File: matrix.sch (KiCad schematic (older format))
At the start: 179 parts, among them SW1.1 Backtick, SW1.10 9, SW1.11 0, SW1.12 -, SW1.13 =, SW1.2 1, SW1.3 2, SW1.4 3, SW1.5 4, SW1.6 5, SW1.7 6, SW1.8 7, SW1.9 8, SW2A1 Tab, SW2A10 I, SW2A11 O, SW2A12 P, SW2A13 /, SW2A2 Q, SW2A3 W, SW2A4 E, SW2A5 R, SW2A6 T, SW2A8 Y, SW2A9 U, SW2B1 Tab, SW2B10 I, SW2B11 O, SW2B12 P, SW2B13 /, SW2B2 Q, SW2B3 W, SW2B4 E, SW2B5 R, SW2B6 T, SW2B7 Y, SW2B8 Y, SW2B9 U, SW3A1 Bksp, SW3A10 K, SW3A11 L, SW3A12 ;, SW3A13 Enter, SW3A2 A, SW3A3 S, SW3A4 D, SW3A5 F, SW3A6 G, SW3A8 H, SW3A9 J, SW3B1 Bksp, SW3B10 K, SW3B11 L, SW3B12 ;, SW3B13 Enter, SW3B2 A, SW3B3 S, SW3B4 D, SW3B5 F, SW3B6 G, SW3B7 H, SW3B8 H, SW3B9 J, SW4A1 LShift, SW4A10 ,, SW4A11 ., SW4A13 RShift, SW4A3 Z, SW4A4 X, SW4A5 C, SW4A6 V, SW4A8 N, SW4A9 M, SW4B1 LShift, SW4B10 ,, SW4B11 ., SW4B12 ., SW4B13 RShift, SW4B2 Z, SW4B3 Z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

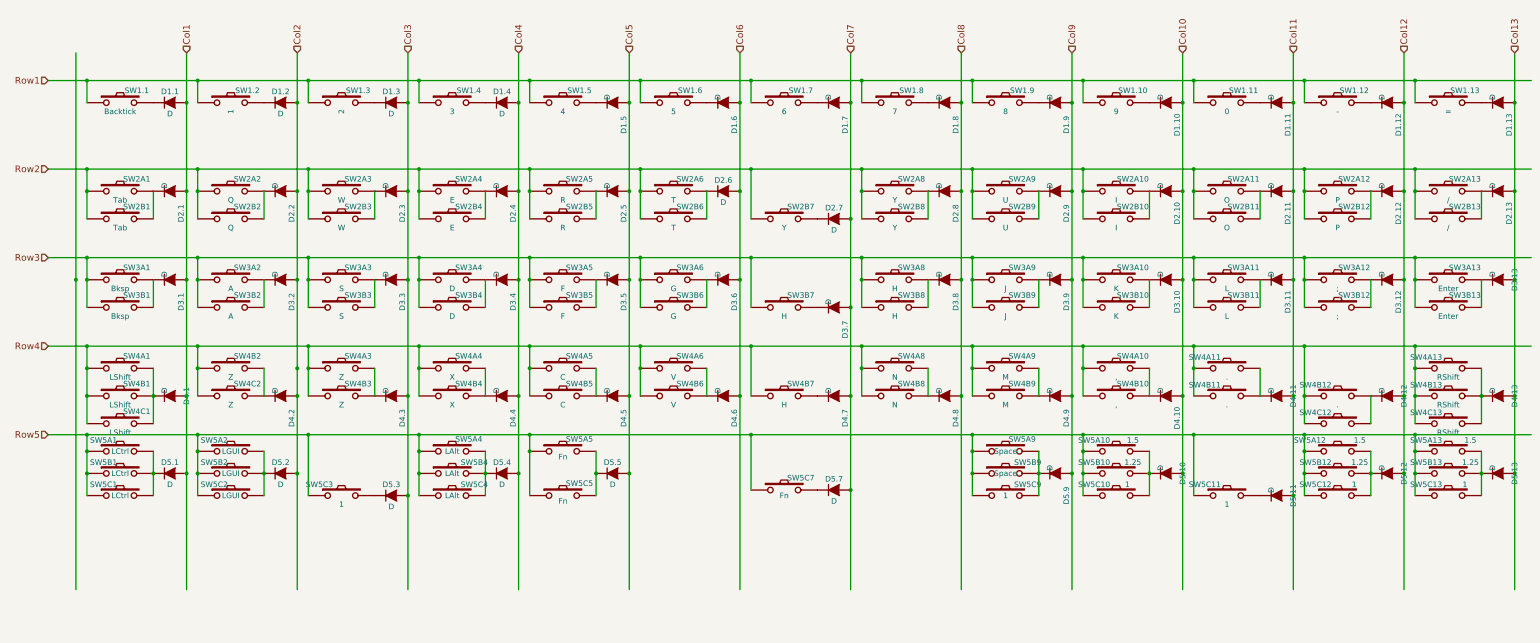
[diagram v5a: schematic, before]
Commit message: Focusing efforts on one main layout (semi-ortho), so that PCB-mounted and Alps components can be supported
Updated keenkeeb-reb1.png with new layout.
Started removing footprints and adding new spacebar footprints.
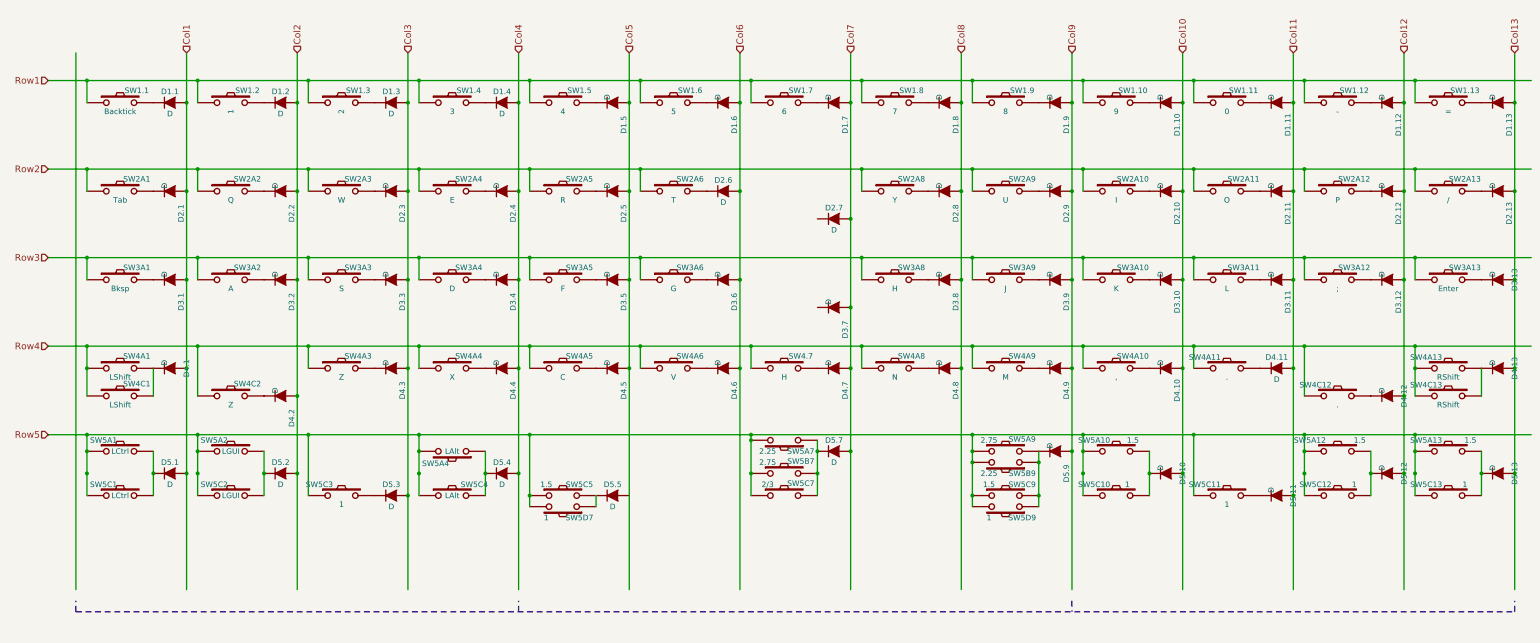
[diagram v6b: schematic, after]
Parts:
- removed SW2B1: Tab, footprints:MX_100_Plate, symbol SW_PUSH
- removed SW2B10: I, footprints:MX_100_Plate, symbol SW_PUSH
- removed SW2B11: O, footprints:MX_100_Plate, symbol SW_PUSH
- removed SW2B12: P, footprints:MX_100_Plate, symbol SW_PUSH
- removed SW2B13: /, footprints:MX_100_Plate, symbol SW_PUSH
- removed SW2B2: Q, footprints:MX_100_Plate, symbol SW_PUSH
- removed SW2B3: W, footprints:MX_100_Plate, symbol SW_PUSH
- removed SW2B4: E, footprints:MX_100_Plate, symbol SW_PUSH
- removed SW2B5: R, footprints:MX_100_Plate, symbol SW_PUSH
- removed SW2B6: T, footprints:MX_100_Plate, symbol SW_PUSH
- removed SW2B7, SW2B8: Y, footprints:MX_100_Plate, symbol SW_PUSH
- removed SW2B9: U, footprints:MX_100_Plate, symbol SW_PUSH
- removed SW3B1: Bksp, footprints:MX_100_Plate, symbol SW_PUSH
- removed SW3B10: K, footprints:MX_100_Plate, symbol SW_PUSH
- removed SW3B11: L, footprints:MX_100_Plate, symbol SW_PUSH
- removed SW3B12: ;, footprints:MX_100_Plate, symbol SW_PUSH
- removed SW3B13: Enter, footprints:MX_100_Plate, symbol SW_PUSH
- removed SW3B2: A, footprints:MX_100_Plate, symbol SW_PUSH
- removed SW3B3: S, footprints:MX_100_Plate, symbol SW_PUSH
- removed SW3B4: D, footprints:MX_100_Plate, symbol SW_PUSH
- removed SW3B5: F, footprints:MX_100_Plate, symbol SW_PUSH
- removed SW3B6: G, footprints:MX_100_Plate, symbol SW_PUSH
- removed SW3B7, SW3B8: H, footprints:MX_100_Plate, symbol SW_PUSH
- removed SW3B9: J, footprints:MX_100_Plate, symbol SW_PUSH
- removed SW4B1: LShift, footprints:MX_150_Plate, symbol SW_PUSH
- removed SW4B10: ,, footprints:MX_100_Plate, symbol SW_PUSH
- removed SW4B11, SW4B12: ., footprints:MX_100_Plate, symbol SW_PUSH
- removed SW4B13: RShift, footprints:MX_150_Plate, symbol SW_PUSH
- removed SW4B3, SW4C2: Z, footprints:MX_100_Plate, symbol SW_PUSH
- removed SW4B4: X, footprints:MX_100_Plate, symbol SW_PUSH
- removed SW4B5: C, footprints:MX_100_Plate, symbol SW_PUSH
- removed SW4B6: V, footprints:MX_100_Plate, symbol SW_PUSH
- removed SW4B8: N, footprints:MX_100_Plate, symbol SW_PUSH
- removed SW4B9: M, footprints:MX_100_Plate, symbol SW_PUSH
- removed SW5B1: LCtrl, footprints:MX_125_Plate, symbol SW_PUSH
- removed SW5B10, SW5B12, SW5B13: 1.25, footprints:MX_125_Plate, symbol SW_PUSH
- removed SW5B2: LGUI, footprints:MX_125_Plate, symbol SW_PUSH
- removed SW5B4: LAlt, footprints:MX_125_Plate, symbol SW_PUSH
- added SW5C5: 1.5, footprints:MX_150_Plate, symbol SW_PUSH
- added SW5D7, SW5D9: 1, footprints:MX_100_Plate, symbol SW_PUSH
- SW5A7: renamed from SW5A5; value Fn -> 2.25
- SW5A9: value Space -> 2.75
- SW5B7: renamed from SW5C5; value Fn -> 2.75; footprint footprints:MX_200_Plate_NoStabHoles -> footprints:MX_275_Plate_NoStabHoles
- SW5B9: value Space -> 2.25; footprint footprints:MX_275_Plate_NoStabHoles -> footprints:MX_225_Plate_NoStabHoles
- SW5C7: value Fn -> 2/3
- SW5C9: value 1 -> 1.5; footprint footprints:MX_100_Plate -> footprints:MX_150_Plate
- renumbered SW4B7 to SW4.7, SW4B2 to SW4C2
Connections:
- wire segments 126 -> 91
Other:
- moved on the sheet: D4.1, D4.10, D4.11, D4.13, D4.3, D4.4, D4.5, D4.6, D4.7, D4.8, D4.9, D5.5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

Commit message: Started to layout with MX/Alps footprints
Added footprints that support Cherry MX and Alps switches.
Started to layout the board with new footprints.  Will support PCB
mounted switches/stabs.
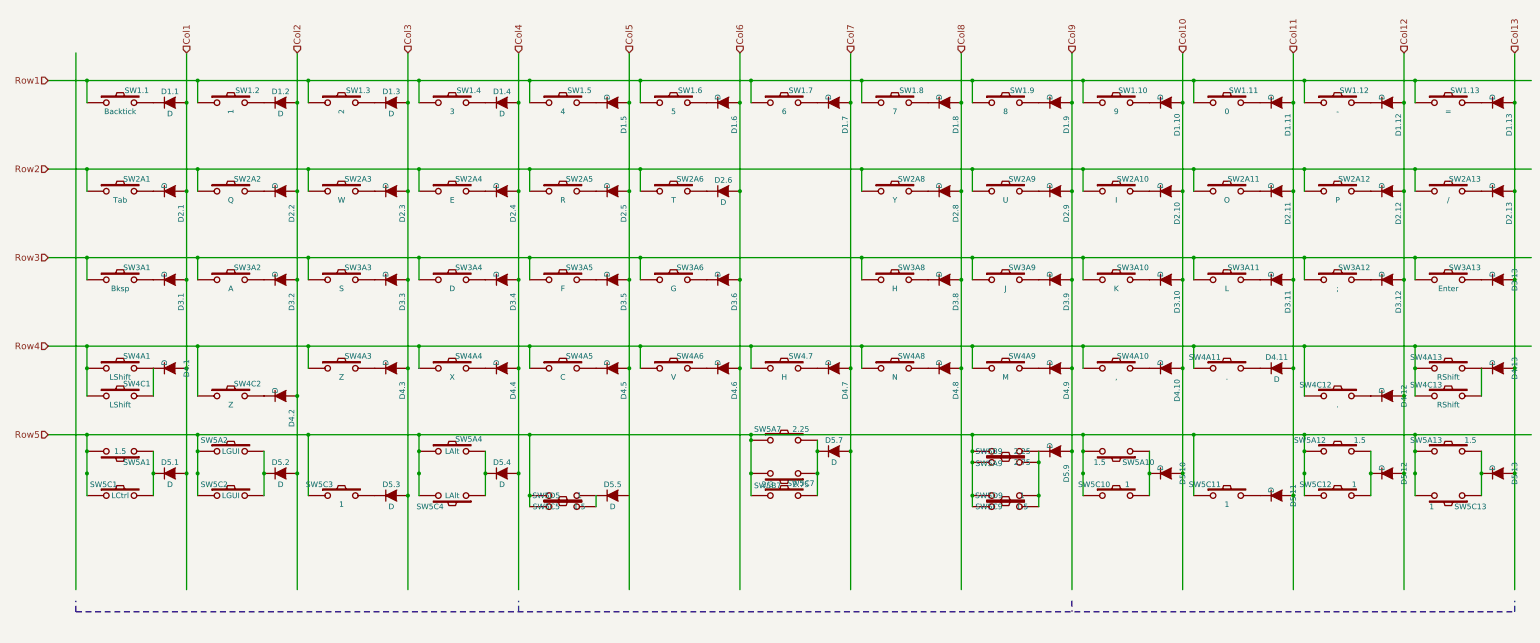
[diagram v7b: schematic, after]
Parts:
- removed D2.7, D3.7: D, Diodes_SMD:D_SOD-323_HandSoldering, symbol D
- SW1.1, SW1.10, SW1.11, SW1.12, SW1.13, SW1.2, SW1.3, SW1.4, SW1.5, SW1.6, SW1.7, SW1.8, SW1.9, SW2A10, SW2A11, SW2A12, SW2A2, SW2A3, SW2A4, SW2A5, SW2A6, SW2A8, SW2A9, SW3A10, SW3A11, SW3A12, SW3A2, SW3A3, SW3A4, SW3A5, SW3A6, SW3A8, SW3A9, SW4.7, SW4A10, SW4A11, SW4A3, SW4A4, SW4A5, SW4A6, SW4A8, SW4A9, SW4C1, SW4C12, SW4C13, SW4C2, SW5A12, SW5A2, SW5C1, SW5C10, SW5C11, SW5C12, SW5C13, SW5C2, SW5C3, SW5C4, SW5D9: footprint footprints:MX_100_Plate -> footprints:Mx_Alps_100
- SW2A1, SW2A13, SW3A1, SW3A13, SW5A10, SW5A13, SW5A4, SW5C5, SW5C9: footprint footprints:MX_150_Plate -> footprints:Mx_Alps_150
- SW4A1, SW4A13, SW5C7: footprint footprints:MX_200_Plate_NoStabHoles -> footprints:Mx_Alps_200
- SW5A1: value LCtrl -> 1.5; footprint footprints:MX_150_Plate -> footprints:Mx_Alps_150
- SW5A7, SW5B9: footprint footprints:MX_225_Plate_NoStabHoles -> footprints:Mx_Alps_225
- SW5A9, SW5B7: footprint footprints:MX_275_Plate_NoStabHoles -> footprints:Mx_Alps_275
- SW5D5: renamed from SW5D7; footprint footprints:MX_100_Plate -> footprints:Mx_Alps_100
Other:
- moved on the sheet: SW5A1, SW5A10, SW5A4, SW5A7, SW5A9, SW5B7, SW5B9, SW5C13, SW5C4, SW5C5, SW5C9, SW5D5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

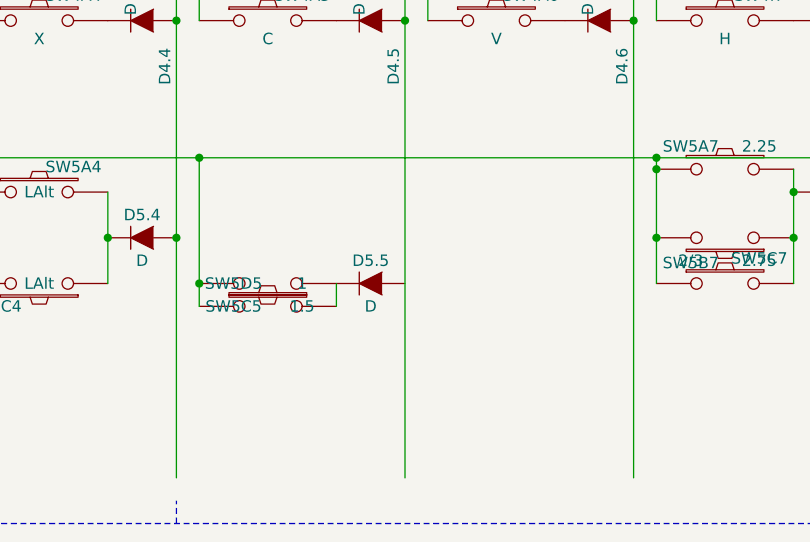
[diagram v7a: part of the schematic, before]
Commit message: Connected most of the components on the board
TODO:
Replace P1 with 1x6 header for SPI, Vcc, GND
Add test pads
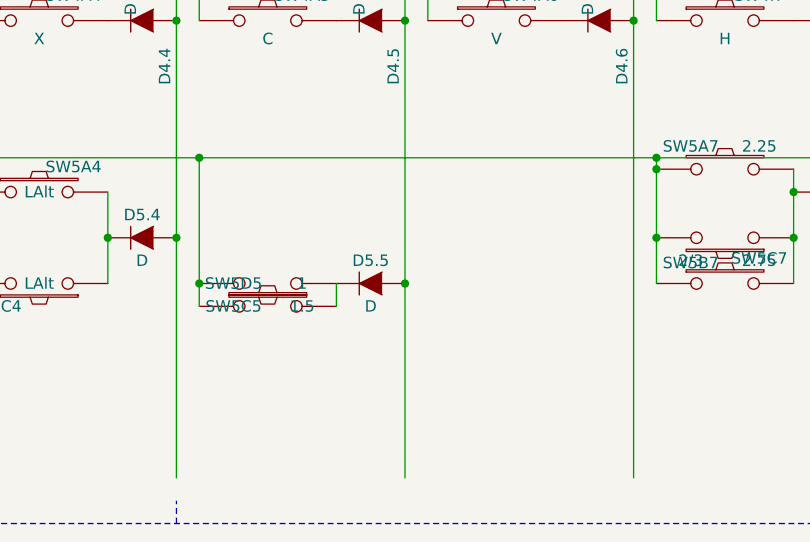
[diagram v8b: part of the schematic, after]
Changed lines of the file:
@@
 Wire Notes Line
 	2300 6700 2300 6600
+Connection ~ 7300 5650
 $EndSCHEMATC
